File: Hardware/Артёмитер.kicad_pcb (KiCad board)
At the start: 4 copper layers, 54.5 x 18 mm, 103 parts, among them IC2 AS5F32G04SNDA-08LIN, J1 Conn_01x04_Male, J2 Conn_01x02_Male, J3 USB_C_Receptacle_USB2.0, J4 Conn_01x02_Male, Q1 PMV20ENR, U1 150044M155220, U10 MAX77827AEFD+T, U11 SC4215, U2 ESP32-S3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

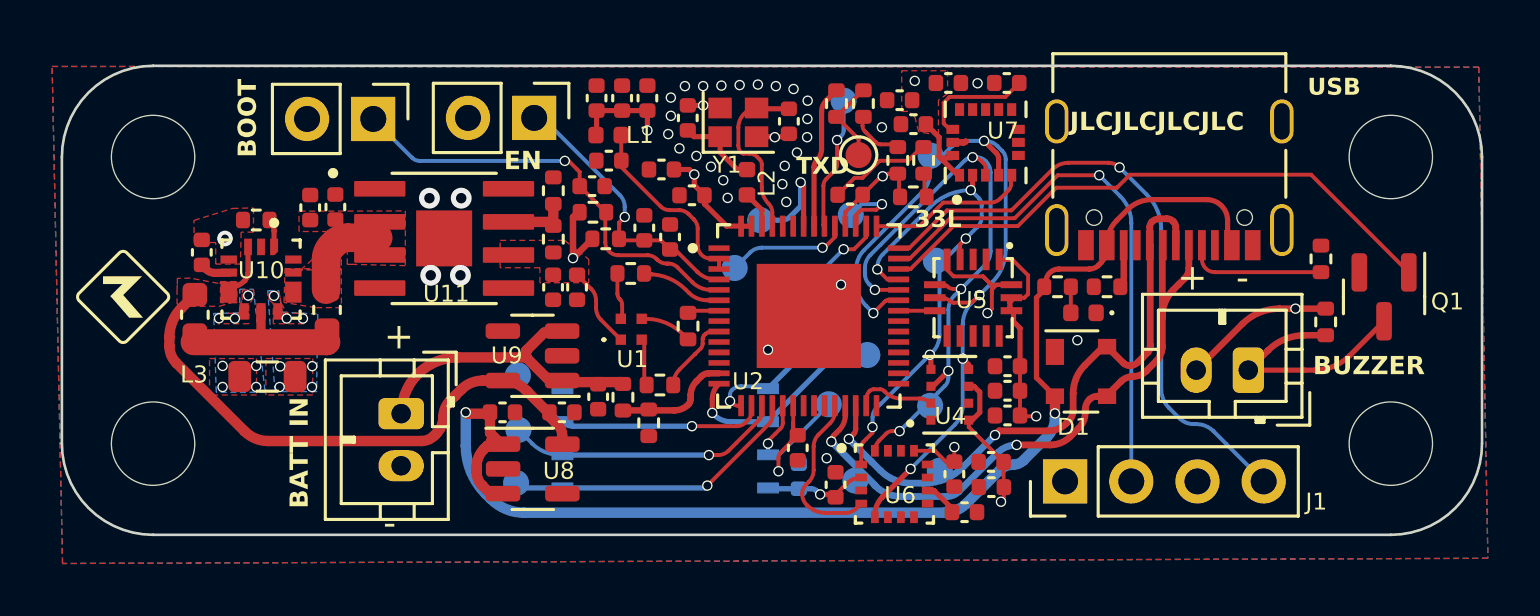
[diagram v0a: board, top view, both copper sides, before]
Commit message: code on altimeter during flight
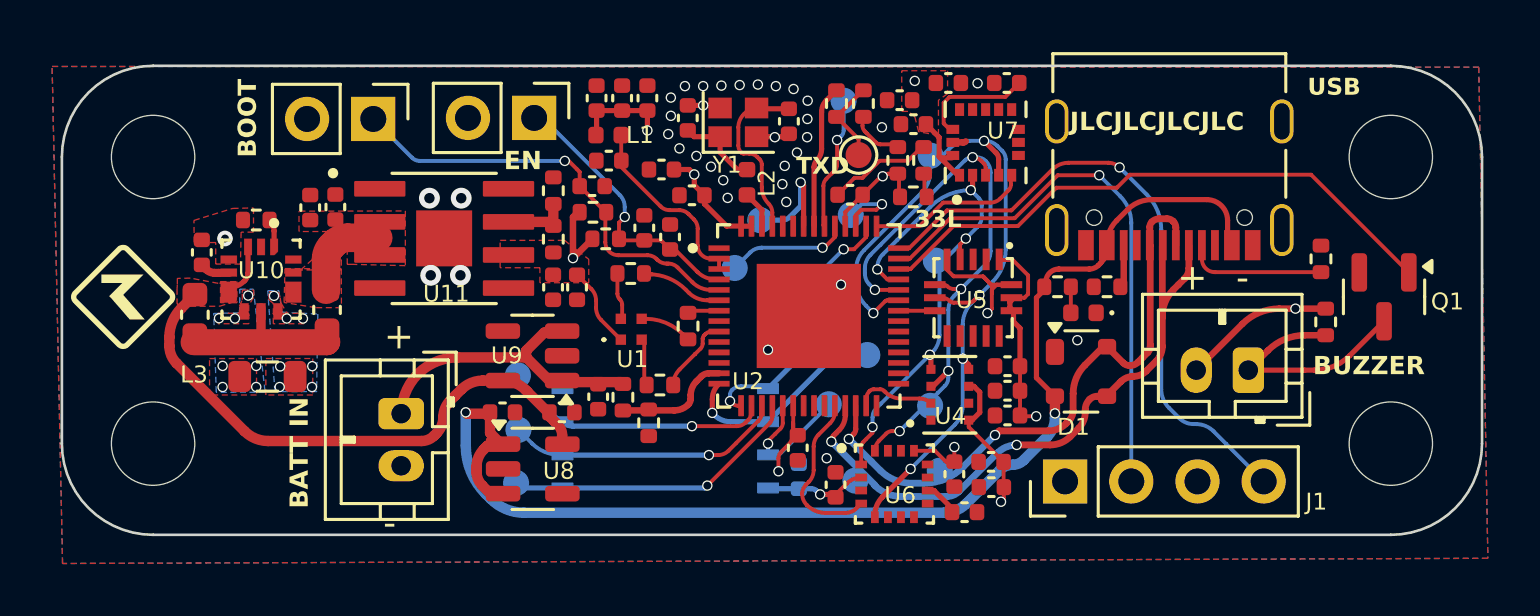
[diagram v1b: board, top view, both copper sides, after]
